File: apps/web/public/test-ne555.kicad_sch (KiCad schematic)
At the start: 9 parts, among them J1 PWR_5V, U1 NE555P

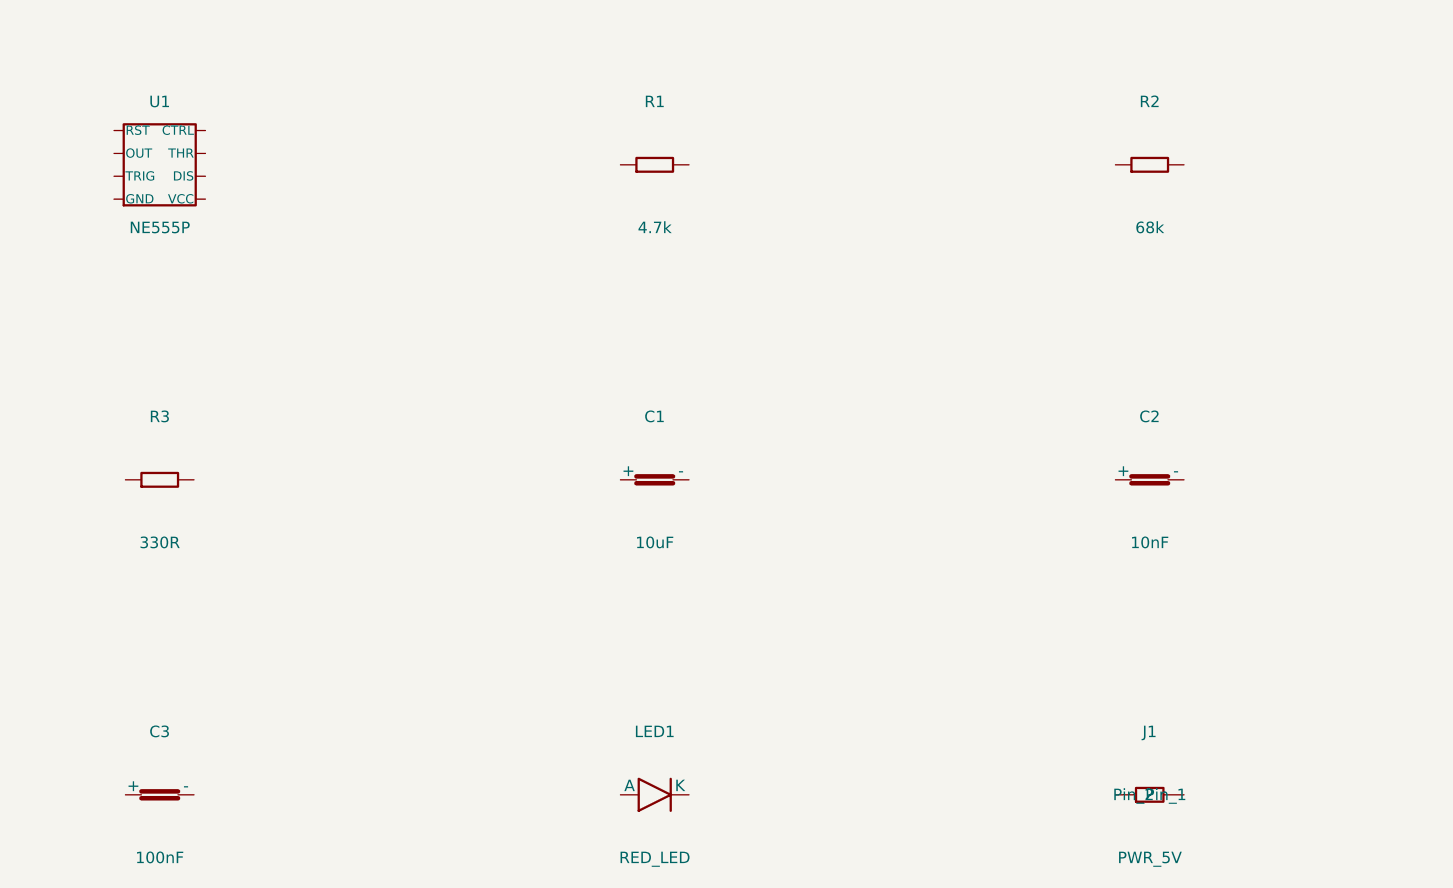
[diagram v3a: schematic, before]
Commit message: fix(schematic): add 20mm side margin to clear inner frame border
Components U1/J1 (left column) and far-right components were drawn
on top of the KiCad inner frame vertical borders (at x=10mm from
paper edge). The previous 12mm margin_side only gave 2mm clearance.

Changes:
- margin_side 12 -> 20mm in _build_flat_schematic_with_net_labels()
  (gives 10mm clearance from inner frame on both sides)
- Regenerated test-lm7805 / test-ne555 / test-esp32 .kicad_sch via
  /circuit-synth/generate (paper width 149 -> 165mm as a result)
- test-cs.html: ResizeObserver on canvas + window load/resize retries
  to reapply auto-zoom when KiCanvas resets its camera on layout
  changes (fixes title block peeking before click-to-interact)

Verified via Chrome DevTools screenshots on all 3 schematic tabs.
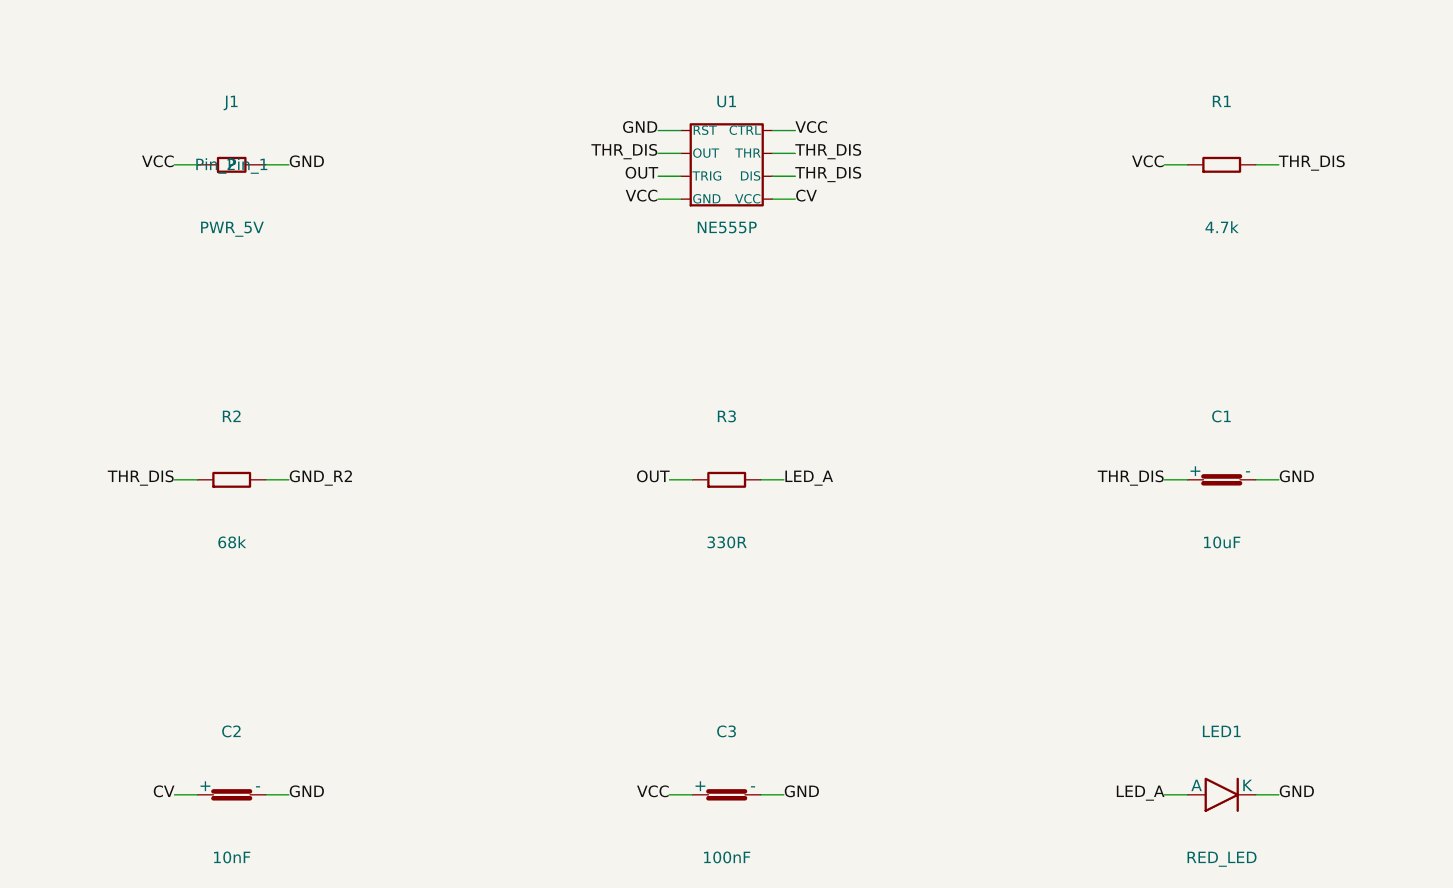
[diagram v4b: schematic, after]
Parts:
- C1: footprint Capacitor_THT:C_Disc_D5.0mm_W2.5mm_P5.00mm -> Capacitor_SMD:C_1206_3216Metric
- C2, C3: footprint Capacitor_THT:C_Disc_D5.0mm_W2.5mm_P5.00mm -> Capacitor_SMD:C_0603_1608Metric
- LED1: footprint LED_THT:LED_D5.0mm -> LED_SMD:LED_0603_1608Metric
- R1, R2, R3: footprint Resistor_THT:R_Axial_DIN0207_L6.3mm_D2.5mm_P10.16mm_Horizontal -> Resistor_SMD:R_0603_1608Metric
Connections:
- net OUT: now reaches R3.1
- net OUT: now also U1.2 (TRIG)
- net LED_A: now reaches R3.2
- net LED_A: now also LED1.1 (A)
- net VCC: now reaches J1.1 (Pin_1)
- net VCC: now also C3.1 (+), R1.1, U1.1 (GND), U1.5 (CTRL)
- net GND: now reaches J1.2 (Pin_2)
- net GND: now also C1.2 (-), C2.2 (-), C3.2 (-), LED1.2 (K), U1.4 (RST)
- net CV: now reaches C2.1 (+)
- net CV: now also U1.8 (VCC)
- net THR_DIS: now reaches C1.1 (+)
- net THR_DIS: now also R1.2, R2.1, U1.3 (OUT), U1.6 (THR), U1.7 (DIS)
- net GND_R2: now reaches R2.2

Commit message: fix(schematic): bump margin_side to 28mm so net-label text stays inside frame
Previous 20mm margin put component body 10mm inside the inner frame,
but net-label text ("VIN", "VOUT", "GND"...) extends ~8mm left/right
of the body — so label text sat only ~3mm from the inner frame border,
looking cramped.

New 28mm margin_side accounts for the 8mm label overhang:
  component body at x=28mm
  label text reaches x=28-8=20mm
  inner frame at x=10mm
  -> 10mm visual clearance between label text and frame border

Paper width grows 165 -> 181mm. Regenerated all 3 test schematics.
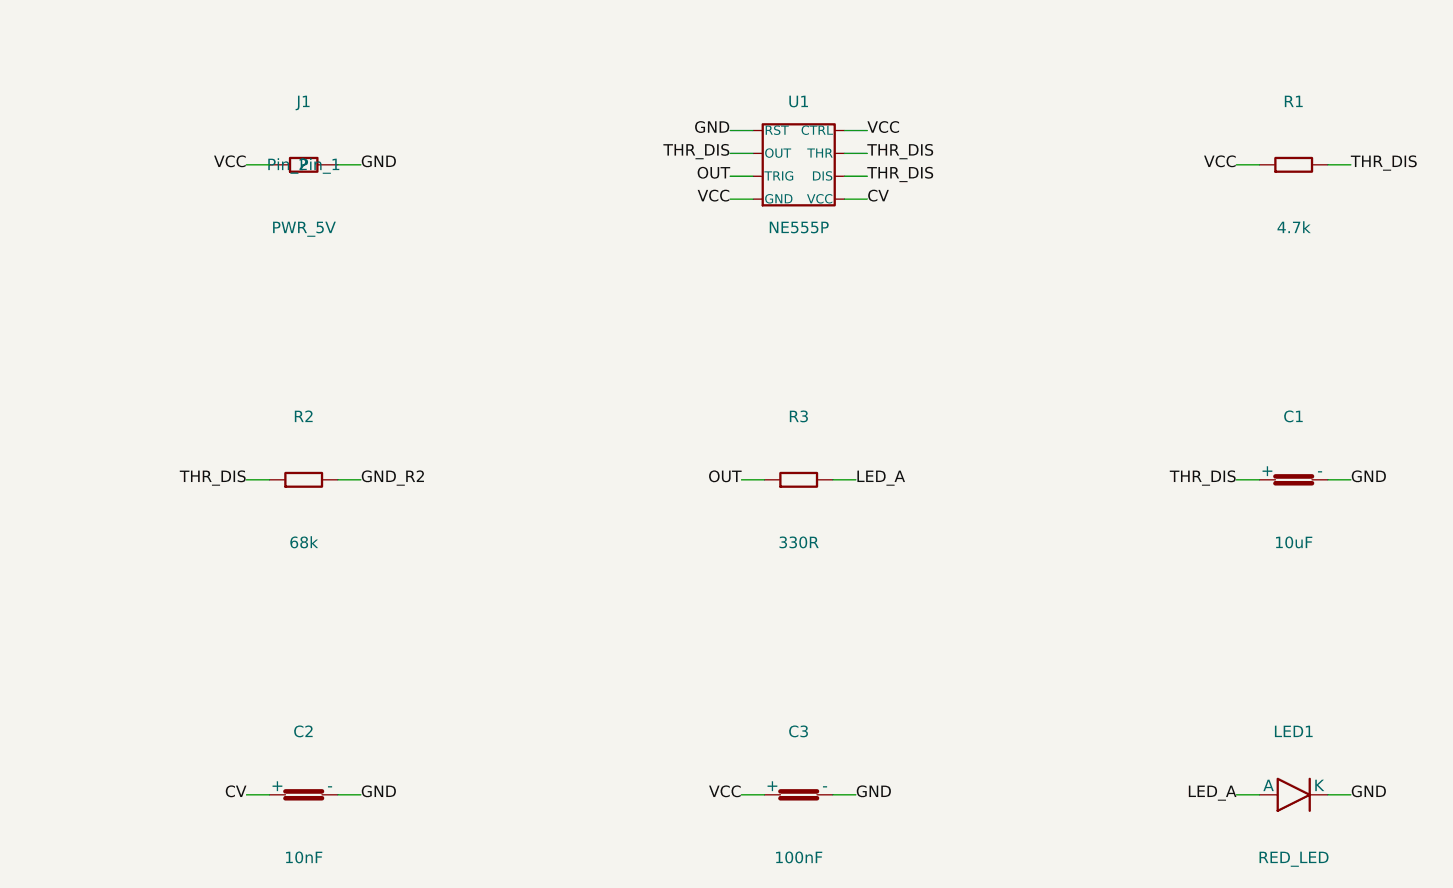
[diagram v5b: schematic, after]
